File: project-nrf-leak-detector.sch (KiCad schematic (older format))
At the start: 16 parts, among them J1 Conn_02x05_Odd_Even, J2 Water Probe, Q1 Q_NMOS_GSD, U1 MS88SF3_NRF52840

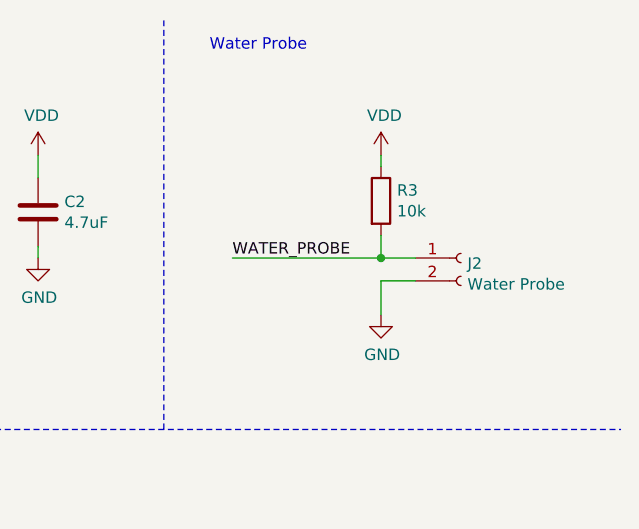
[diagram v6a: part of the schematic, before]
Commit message: Add a cap on the probe signal
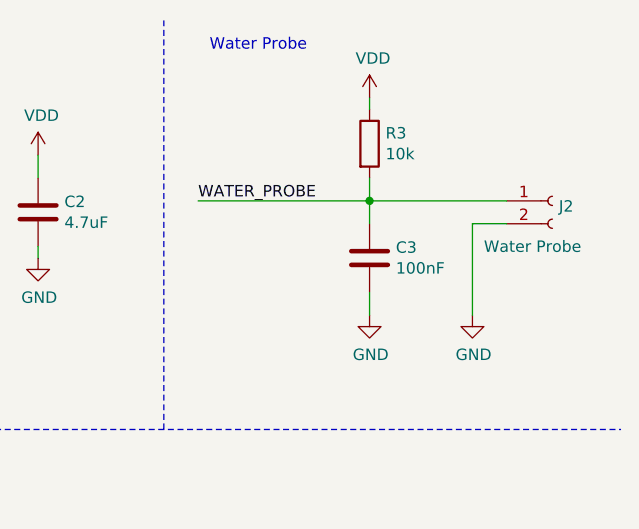
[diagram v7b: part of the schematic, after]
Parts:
- added C3: 100nF, Capacitor_SMD:C_0603_1608Metric, symbol Device:C
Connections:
- net GND: now also C3.2
- net WATER_PROBE: now also C3.1
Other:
- moved on the sheet: J2, R3
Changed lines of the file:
@@
 L power:GND #PWR0106
 U 1 1 639069CC
-P 10150 1800
-F 0 "#PWR0106" H 10150 1550 50  0001 C CNN
-F 1 "GND" H 10155 1627 50  0000 C CNN
-F 2 "" H 10150 1800 50  0001 C CNN
-F 3 "" H 10150 1800 50  0001 C CNN
-	1    10150 1800
-	1    0    0    -1
-$EndComp
-Wire Wire Line
-	10150 1800 10150 1650
+P 10550 1800
+F 0 "#PWR0106" H 10550 1550 50  0001 C CNN
+F 1 "GND" H 10555 1627 50  0000 C CNN
+F 2 "" H 10550 1800 50  0001 C CNN
+F 3 "" H 10550 1800 50  0001 C CNN
+	1    10550 1800
+	1    0    0    -1
+$EndComp
+Wire Wire Line
+	10550 1800 10550 1400
 Wire Wire Line
 	4250 1300 4250 1400
@@
 L Device:R R3
 U 1 1 63F7A9F2
-P 10150 1300
-F 0 "R3" H 10220 1346 50  0000 L CNN
-F 1 "10k" H 10220 1255 50  0000 L CNN
-F 2 "Resistor_SMD:R_0603_1608Metric" V 10080 1300 50  0001 C CNN
-F 3 "~" H 10150 1300 50  0001 C CNN
-	1    10150 1300
-	1    0    0    -1
-$EndComp
-Wire Wire Line
-	10150 1100 10150 1150
-Wire Wire Line
-	10150 1650 10300 1650
+P 10100 1050
+F 0 "R3" H 10170 1096 50  0000 L CNN
+F 1 "10k" H 10170 1005 50  0000 L CNN
+F 2 "Resistor_SMD:R_0603_1608Metric" V 10030 1050 50  0001 C CNN
+F 3 "~" H 10100 1050 50  0001 C CNN
+	1    10100 1050
+	1    0    0    -1
+$EndComp
+Wire Wire Line
+	10100 850  10100 900
+Wire Wire Line
+	10550 1400 10700 1400
 $Comp
 L Connector:Conn_01x02_Female J2
 U 1 1 637340AC
-P 10500 1550
-F 0 "J2" H 10528 1526 50  0000 L CNN
-F 1 "Water Probe" H 10528 1435 50  0000 L CNN
-F 2 "TZ022101B000G:TZ022101B000G" H 10500 1550 50  0001 C CNN
-F 3 "~" H 10500 1550 50  0001 C CNN
-	1    10500 1550
-	1    0    0    -1
-$EndComp
-Text Label 9500 1550 0    50   ~ 0
+P 10900 1300
+F 0 "J2" H 10928 1276 50  0000 L CNN
+F 1 "Water Probe" H 10600 1100 50  0000 L CNN
+F 2 "TZ022101B000G:TZ022101B000G" H 10900 1300 50  0001 C CNN
+F 3 "~" H 10900 1300 50  0001 C CNN
+	1    10900 1300
+	1    0    0    -1
+$EndComp
+Text Label 9350 1300 0    50   ~ 0
 WATER_PROBE
 Wire Wire Line
-	9500 1550 10150 1550
-Wire Wire Line
-	10150 1450 10150 1550
-Connection ~ 10150 1550
-Wire Wire Line
-	10150 1550 10300 1550
+	10100 1200 10100 1300
 $Comp
 L power:VDD #PWR0108
@@
 L power:VDD #PWR0110
 U 1 1 63FE65CA
-P 10150 1100
-F 0 "#PWR0110" H 10150 950 50  0001 C CNN
-F 1 "VDD" H 10165 1273 50  0000 C CNN
-F 2 "" H 10150 1100 50  0001 C CNN
-F 3 "" H 10150 1100 50  0001 C CNN
-	1    10150 1100
+P 10100 850
+F 0 "#PWR0110" H 10100 700 50  0001 C CNN
+F 1 "VDD" H 10115 1023 50  0000 C CNN
+F 2 "" H 10100 850 50  0001 C CNN
+F 3 "" H 10100 850 50  0001 C CNN
+	1    10100 850
 	1    0    0    -1
 $EndComp
@@
 Wire Wire Line
 	650  2900 1200 2900
+$Comp
+L Device:C C3
+U 1 1 640F354A
+P 10100 1550
+F 0 "C3" H 10215 1596 50  0000 L CNN
+F 1 "100nF" H 10215 1505 50  0000 L CNN
+F 2 "Capacitor_SMD:C_0603_1608Metric" H 10138 1400 50  0001 C CNN
+F 3 "~" H 10100 1550 50  0001 C CNN
+	1    10100 1550
+	1    0    0    -1
+$EndComp
+Wire Wire Line
+	10100 1300 10100 1400
+$Comp
+L power:GND #PWR02
+U 1 1 6410454C
+P 10100 1800
+F 0 "#PWR02" H 10100 1550 50  0001 C CNN
+F 1 "GND" H 10105 1627 50  0000 C CNN
+F 2 "" H 10100 1800 50  0001 C CNN
+F 3 "" H 10100 1800 50  0001 C CNN
+	1    10100 1800
+	1    0    0    -1
+$EndComp
+Wire Wire Line
+	10100 1700 10100 1800
+Connection ~ 10100 1300
+Wire Wire Line
+	10100 1300 10700 1300
+Wire Wire Line
+	9350 1300 10100 1300
 $EndSCHEMATC
